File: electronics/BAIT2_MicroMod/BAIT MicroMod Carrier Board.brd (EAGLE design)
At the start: 92.7 x 80 mm, 142 parts, among them J1 SJ-43516-SMT, J10 QWIIC_RIGHT_ANGLE, J15 BM05B-SRSS-TB(LF)(SN), J2 ST-TF-003A, J4 BM05B-SRSS-TB(LF)(SN), J5 QWIIC_RIGHT_ANGLE, J6 JST 2PH, J7 MICROMOD-2222-C, SW1 SKQGADE010, SW2 SKQGADE010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

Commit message: Also removed LR_SEL from MicroMod schematic
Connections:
- removed net LR_SEL: J7.73
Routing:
- net LR_SEL: track 12.5 -> 0.00 mm
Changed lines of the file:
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@@
 <wire x1="63.107" y1="50.431" x2="63.107" y2="48.26" width="0.2032" layer="1"/>
-</signal>
-<signal name="LR_SEL">
-<contactref element="J7" pad="73"/>
-<wire x1="23" y1="49.335" x2="22.904" y2="49.239" width="0.2032" layer="1"/>
-<wire x1="22.904" y1="49.239" x2="22.904" y2="48.4547875" width="0.2032" layer="1"/>
-<wire x1="22.1278125" y1="47.6786" x2="22.904" y2="48.4547875" width="0.2032" layer="1"/>
-<wire x1="12.145" y1="48.801" x2="13.2674" y2="47.6786" width="0.2032" layer="1"/>
-<wire x1="13.2674" y1="47.6786" x2="22.1278125" y2="47.6786" width="0.2032" layer="1"/>
 </signal>
 <signal name="I2S_SCK">

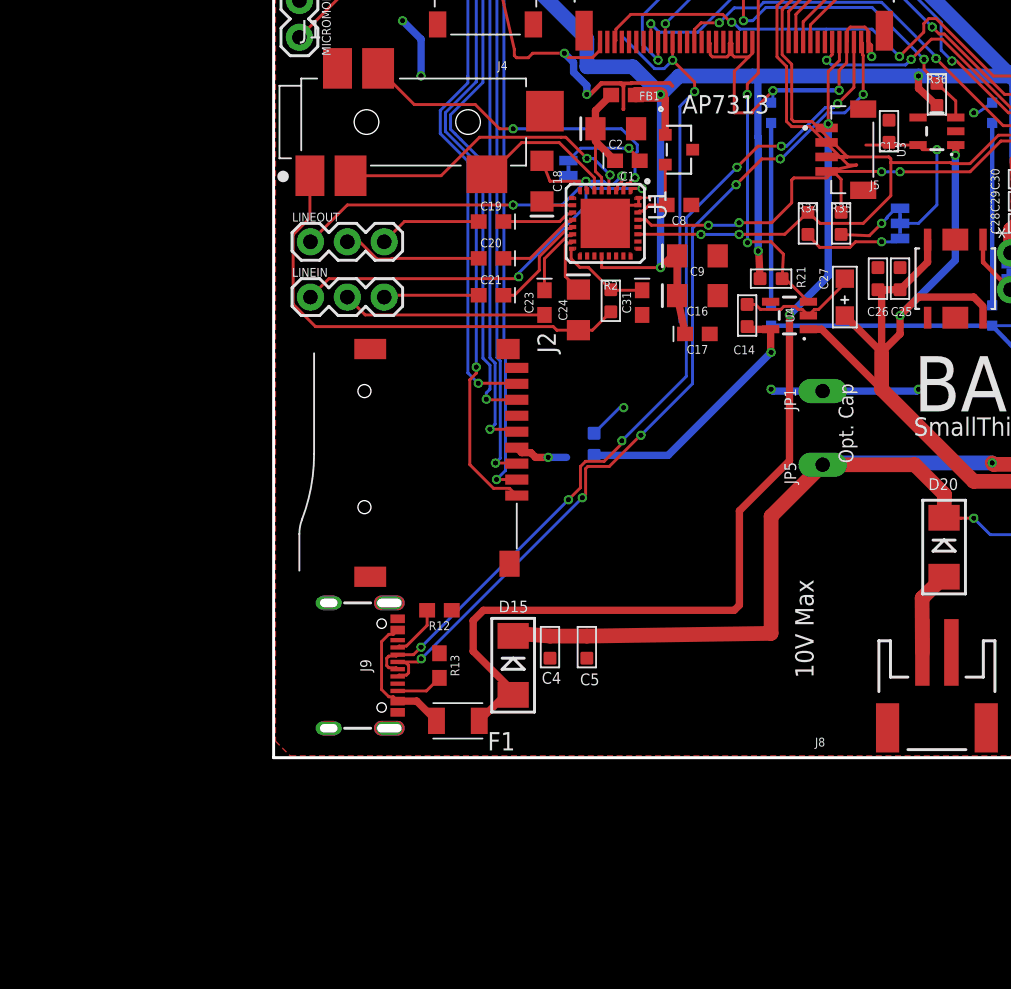
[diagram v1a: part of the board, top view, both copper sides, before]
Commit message: Added 3V3 regulators and options to power direct from 3V3 line
Added a regulator for the SGTL5000 and renamed lines from the SD and qwiic regulators. Added enable lines and jumpers to bypass the regulators if necessary.
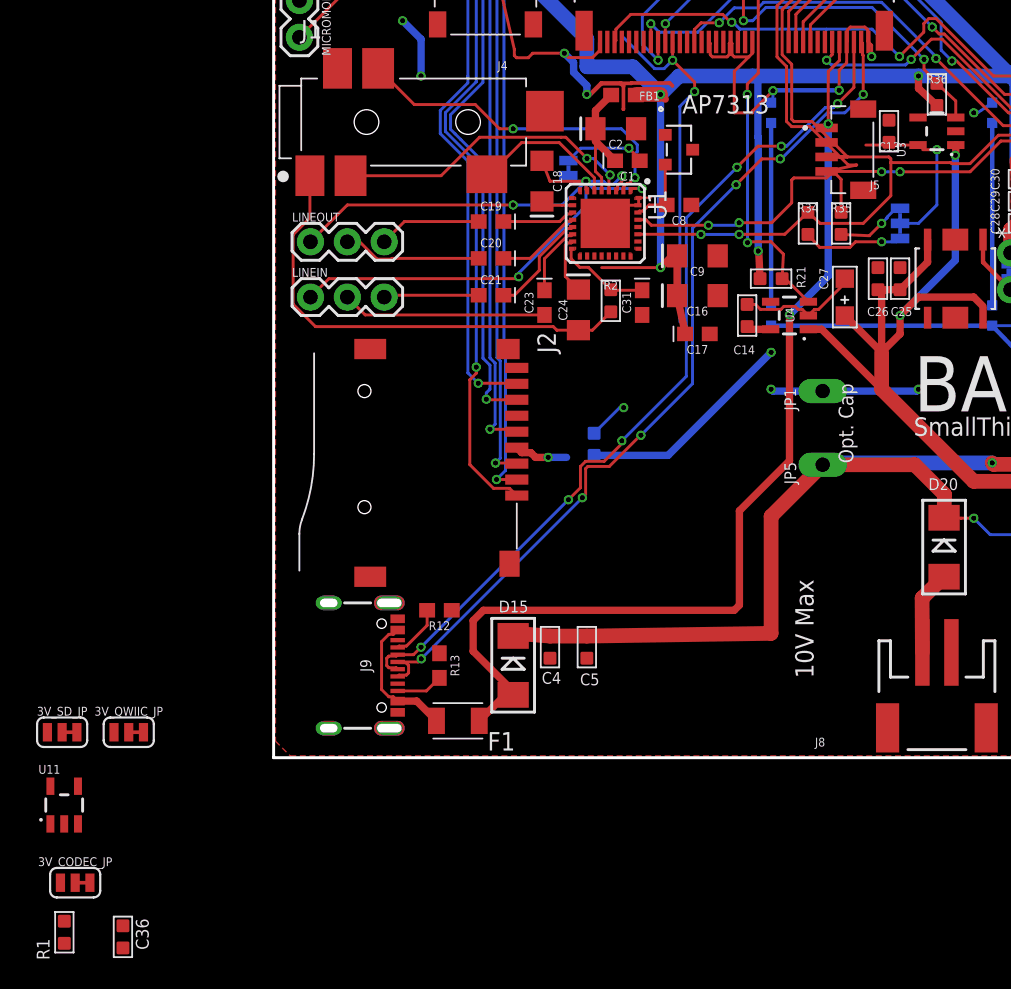
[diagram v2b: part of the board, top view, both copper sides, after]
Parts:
- added 3V_CODEC_JP, 3V_QWIIC_JP, 3V_SD_JP: MK2_LR, SparkFun-Jumpers:SMT-JUMPER_3_1-NC_TRACE_SILK
- added C36: 1uf, OPL_Capacitor:C0603
- added R1: 100K, OPL_Resistor:R0603
- added U11: 3.3V, SparkFun-IC-Power:SOT23-5
- renumbered QWIIC_PWR to QWIIC_PU
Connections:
- net PERIPHERAL_PWR_CTRL renamed SD_EN
- net QWIIC_PWR_CTRL renamed QWIIC_EN
- removed net 3.3V_LP: C14.1, C6.1, J2.4, U4.5
- removed net QWIIC_PWR: C13.1, J5.2, QWIIC_PU.2, U3.5
- new net 3V_CODEC: 3V_CODEC_JP.3, C16.+, C17.+, C9.+, FB1.1, U1.20, U2.1
- new net 3V_QWIIC: 3V_QWIIC_JP.3, J5.2, QWIIC_PU.2
- new net 3V_QWIIC_OUT: 3V_QWIIC_JP.2, C13.1, U3.5
- new net 3V_QWIIC_OUT1: 3V_CODEC_JP.2, C36.1, U11.5
- new net 3V_SD: 3V_SD_JP.3, C6.1, J2.4
- new net 3V_SD_OUT: 3V_SD_JP.2, C14.1, U4.5
- new net CODEC_EN: J7.46, R1.1, U11.3
- net 3.3V: now also 3V_CODEC_JP.1, 3V_QWIIC_JP.1, 3V_SD_JP.1, R1.2; no longer C16.+, C17.+, C9.+, FB1.1, U1.20, U2.1
- net GND: now also C36.2, U11.2
- net V+: now also U11.1
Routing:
- net 3.3V_LP: track 22.2 -> 0.00 mm, vias 2 -> 0
- net 3V_SD: track 0.00 -> 18.9 mm, vias 0 -> 2
- net QWIIC_PWR: track 12.1 -> 0.00 mm, vias 1 -> 0
- net 3.3V: track 265.9 -> 256.8 mm
- net 3V_QWIIC: track 0.00 -> 7.86 mm, vias 0 -> 1
- net 3V_CODEC: track 0.00 -> 5.44 mm
- net 3V_QWIIC_OUT: track 0.00 -> 3.81 mm
- net 3V_SD_OUT: track 0.00 -> 1.43 mm

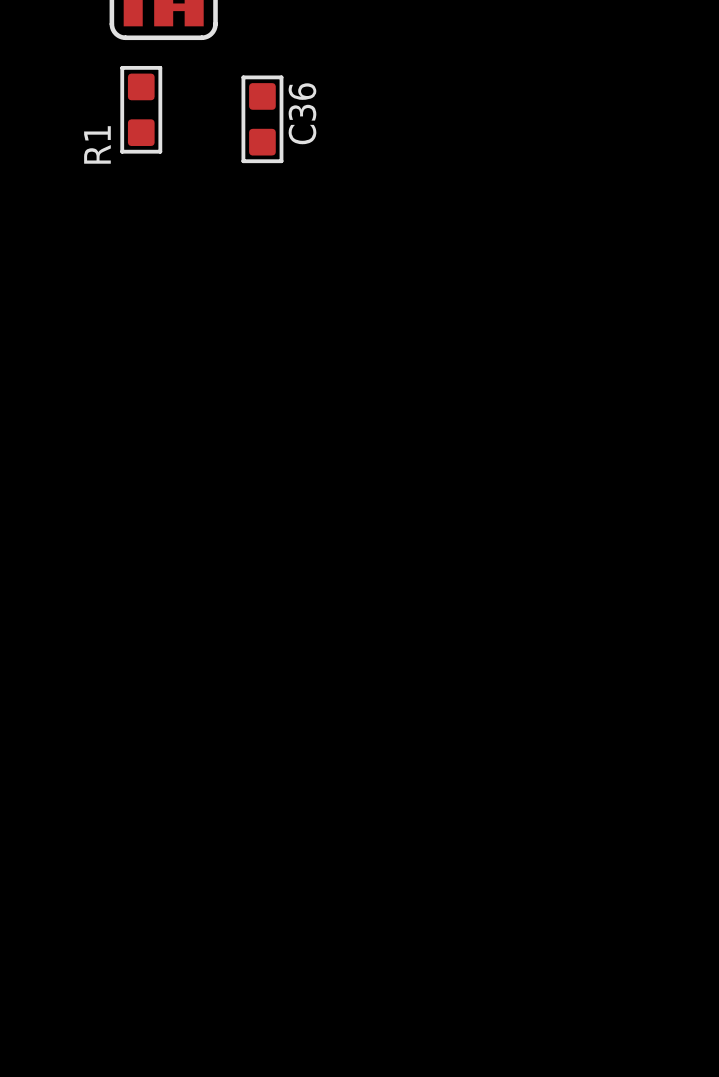
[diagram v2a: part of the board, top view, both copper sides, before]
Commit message: Added second Qwiic port, connected to I2C2 (teensy)
Also added power control for this qwiic
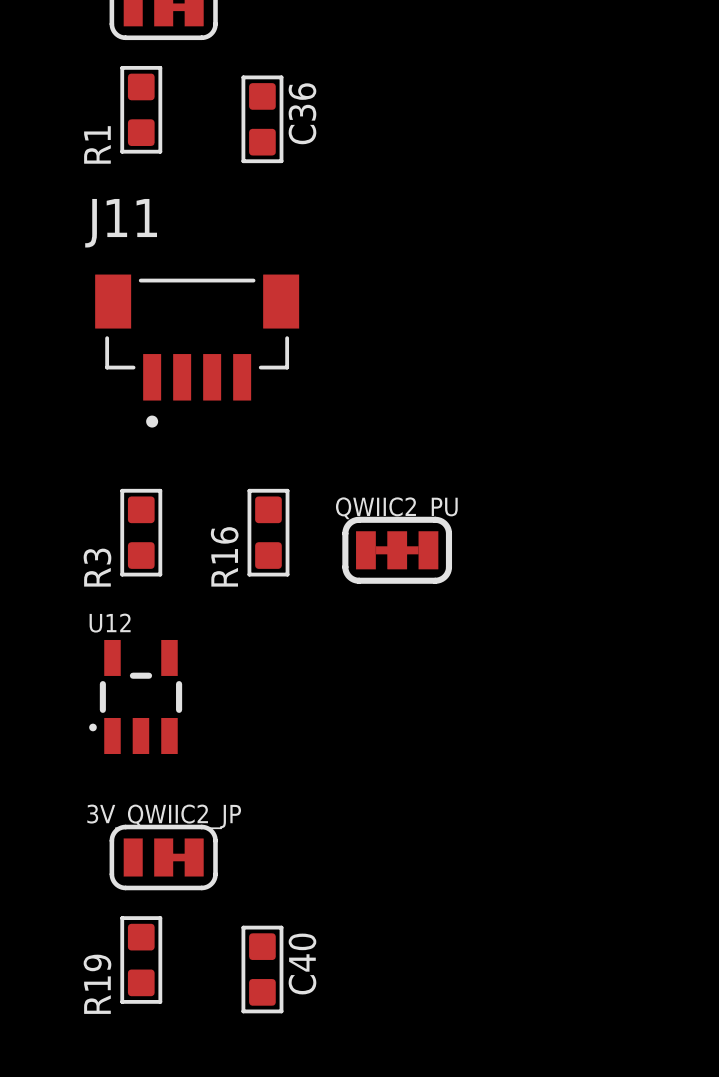
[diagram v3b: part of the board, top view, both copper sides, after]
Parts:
- added 3V_QWIIC2_JP: MK2_LR, SparkFun-Jumpers:SMT-JUMPER_3_1-NC_TRACE_SILK
- added C40: 1uf, OPL_Capacitor:C0603
- added J11: QWIIC_RIGHT_ANGLE, JST SH Connectors:JST_BM04B-SRSS-TB(LF)(SN)
- added QWIIC2_PU: (no value), SparkFun-Jumpers:SMT-JUMPER_3_2-NC_TRACE_SILK
- added R16, R3: 2.2K, OPL_Resistor:R0603
- added R19: 100K, OPL_Resistor:R0603
- added U12: 3.3V, SparkFun-IC-Power:SOT23-5
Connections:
- new net 3V_QWIIC2: 3V_QWIIC2_JP.3, J11.2, QWIIC2_PU.2
- new net 3V_QWIIC_OUT2: 3V_QWIIC2_JP.2, C40.1, U12.5
- new net I2C1_SCL: J11.4, J7.53, R16.1
- new net I2C1_SDA: J7.51
- new net I2C2_SDA: J11.3, R3.1
- new net N$1: QWIIC2_PU.3, R16.2
- new net N$2: QWIIC2_PU.1, R3.2
- new net QWIIC2_EN: J7.46, R19.1, U12.3
- net 3.3V: now also 3V_QWIIC2_JP.1, R19.2
- net CODEC_EN: now also J7.48; no longer J7.46
- net GND: now also C40.2, J11.1, J11.S1, J11.S2, U12.2
- net V+: now also U12.1
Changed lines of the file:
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@@
 <attribute name="VALUE" x="-13.679" y="-9.759" size="0.6096" layer="27" font="vector" ratio="20" align="top-center"/>
+</element>
+<element name="J11" library="JST SH Connectors" library_urn="urn:adsk.eagle:library:41161668" package="JST_BM04B-SRSS-TB(LF)(SN)" package3d_urn="urn:adsk.eagle:package:41161644/2" value="QWIIC_RIGHT_ANGLE" x="-12.564" y="-18.425" smashed="yes">
+<attribute name="AVAILABILITY" value="In Stock" x="-20.398" y="-8.202" size="1.778" layer="27" display="off"/>
+<attribute name="DESCRIPTION" value=" Connector Header Surface Mount 4 position 0.039 (1.00mm) " x="-20.398" y="-8.202" size="1.778" layer="27" display="off"/>
+<attribute name="MF" value="JST Sales" x="-20.398" y="-8.202" size="1.778" layer="27" display="off"/>
+<attribute name="MP" value="BM04B-SRSS-TB(LF)(SN)" x="-20.398" y="-8.202" size="1.778" layer="27" display="off"/>
+<attribute name="MPN" value="BM04B-SRSS-TB(LF)(SN)" x="-20.398" y="-8.202" size="1.778" layer="27" display="off"/>
+<attribute name="NAME" x="-16.214" y="-16.275" size="1.27" layer="25"/>
+<attribute name="PACKAGE" value="None" x="-20.398" y="-8.202" size="1.778" layer="27" display="off"/>
+<attribute name="PRICE" value="None" x="-20.398" y="-8.202" size="1.778" layer="27" display="off"/>
+<attribute name="PURCHASE-URL" value="https://pricing.snapeda.com/search?q=BM04B-SRSS-TB(LF)(SN)&amp;ref=eda" x="-20.398" y="-8.202" size="1.778" layer="27" display="off"/>
+<attribute name="VALUE" x="-16.214" y="-22.975" size="1.27" layer="27" align="top-left"/>
+</element>
+<element name="QWIIC2_PU" library="SparkFun-Jumpers" package="SMT-JUMPER_3_2-NC_TRACE_SILK" package3d_urn="urn:adsk.eagle:package:39289/1" value="" x="-5.896" y="-26.716" smashed="yes">
+<attribute name="NAME" x="-5.896" y="-25.573" size="0.6096" layer="25" font="vector" ratio="20" align="bottom-center"/>
+<attribute name="VALUE" x="-5.896" y="-27.859" size="0.6096" layer="27" font="vector" ratio="20" align="top-center"/>
+</element>
+<element name="R3" library="OPL_Resistor" library_urn="urn:adsk.eagle:library:8004883" package="R0603" package3d_urn="urn:adsk.eagle:package:8004941/1" value="2.2K" x="-14.426" y="-26.129" smashed="yes">
+<attribute name="MPN" value="RC0603JR-072K2L" x="-30.675" y="-12.033" size="1.778" layer="27" display="off"/>
+<attribute name="NAME" x="-15.442" y="-28.034" size="0.889" layer="25" ratio="11" rot="R90"/>
+<attribute name="VALUE" x="-12.991" y="-27.734" size="0.635" layer="27" ratio="10" rot="R90"/>
+</element>
+<element name="R16" library="OPL_Resistor" library_urn="urn:adsk.eagle:library:8004883" package="R0603" package3d_urn="urn:adsk.eagle:package:8004941/1" value="2.2K" x="-10.186" y="-26.129" smashed="yes">
+<attribute name="MPN" value="RC0603JR-072K2L" x="-34.915" y="-12.033" size="1.778" layer="27" display="off"/>
+<attribute name="NAME" x="-11.202" y="-28.034" size="0.889" layer="25" ratio="11" rot="R90"/>
+<attribute name="VALUE" x="-8.751" y="-27.734" size="0.635" layer="27" ratio="10" rot="R90"/>
+</element>
+<element name="C40" library="OPL_Capacitor" library_urn="urn:adsk.eagle:library:8004261" package="C0603" package3d_urn="urn:adsk.eagle:package:8004287/1" value="1uf" x="-10.387" y="-40.69" smashed="yes">
+<attribute name="MPN" value="CC0603KRX7R8BB105" x="-18.892" y="-25.524" size="1.778" layer="27" display="off"/>
+<attribute name="NAME" x="-10.641" y="-39.42" size="0.635" layer="33" ratio="10" rot="R270"/>
+<attribute name="NAME" x="-9.498" y="-39.42" size="0.889" layer="25" ratio="11" rot="R270"/>
+<attribute name="VALUE" x="-11.9745" y="-39.42" size="0.635" layer="27" ratio="10" rot="R270"/>
+</element>
+<element name="R19" library="OPL_Resistor" library_urn="urn:adsk.eagle:library:8004883" package="R0603" package3d_urn="urn:adsk.eagle:package:8004941/1" value="100K" x="-14.426" y="-40.373" smashed="yes">
+<attribute name="MPN" value="RC0603FR-07100KL" x="-22.931" y="-26.129" size="1.778" layer="27" display="off"/>
+<attribute name="NAME" x="-15.442" y="-42.278" size="0.889" layer="25" ratio="11" rot="R90"/>
+<attribute name="VALUE" x="-12.991" y="-41.978" size="0.635" layer="27" ratio="10" rot="R90"/>
+</element>
+<element name="U12" library="SparkFun-IC-Power" package="SOT23-5" value="3.3V" x="-14.436" y="-31.606" smashed="yes">
+<attribute name="NAME" x="-16.214" y="-29.447" size="0.6096" layer="25" ratio="20"/>
+<attribute name="PROD_ID" value="VREG-12457" x="-26.785" y="-25.24" size="1.778" layer="27" display="off"/>
+<attribute name="VALUE" x="-16.214" y="-34.4" size="0.6096" layer="27" ratio="20"/>
+</element>
+<element name="3V_QWIIC2_JP" library="SparkFun-Jumpers" library_urn="urn:adsk.eagle:library:528" package="SMT-JUMPER_3_1-NC_TRACE_SILK" package3d_urn="urn:adsk.eagle:package:39288/1" value="MK2_LR" x="-13.679" y="-36.956" smashed="yes">
+<attribute name="NAME" x="-13.679" y="-35.813" size="0.6096" layer="25" font="vector" ratio="20" align="bottom-center"/>
+<attribute name="VALUE" x="-13.679" y="-38.099" size="0.6096" layer="27" font="vector" ratio="20" align="top-center"/>
 </element>
 </elements>
@@
 <contactref element="C36" pad="2"/>
 <contactref element="U11" pad="2"/>
+<contactref element="J11" pad="1"/>
+<contactref element="J11" pad="S1"/>
+<contactref element="J11" pad="S2"/>
+<contactref element="C40" pad="2"/>
+<contactref element="U12" pad="2"/>
 <wire x1="69.5" y1="63.54" x2="67.25" y2="72.04" width="0" layer="19" extent="1-1"/>
 <wire x1="57.912" y1="73.66" x2="67.25" y2="72.04" width="0" layer="19" extent="1-1"/>
@@
 <wire x1="-14.436" y1="-4.5661" x2="8.55" y2="3.125" width="0" layer="19" extent="1-1"/>
 <wire x1="-10.387" y1="-13.112" x2="-14.436" y2="-4.5661" width="0" layer="19" extent="1-1"/>
+<wire x1="-9.764" y1="-18.425" x2="-10.387" y2="-13.112" width="0" layer="19" extent="1-1"/>
+<wire x1="-14.064" y1="-20.95" x2="-9.764" y2="-18.425" width="0" layer="19" extent="1-1"/>
+<wire x1="-15.364" y1="-18.425" x2="-14.064" y2="-20.95" width="0" layer="19" extent="1-1"/>
+<wire x1="-14.436" y1="-32.9061" x2="-14.064" y2="-20.95" width="0" layer="19" extent="1-1"/>
+<wire x1="-10.387" y1="-41.452" x2="-14.436" y2="-32.9061" width="0" layer="19" extent="1-1"/>
 </signal>
 <signal name="3.3V" class="1">
@@
 <contactref element="R1" pad="2"/>
 <contactref element="3V_CODEC_JP" pad="1"/>
+<contactref element="R19" pad="2"/>
+<contactref element="3V_QWIIC2_JP" pad="1"/>
 <wire x1="-11.004" y1="1.755" x2="22.61" y2="33.782" width="0" layer="19" extent="1-1"/>
 <wire x1="-15.593" y1="1.755" x2="-11.004" y2="1.755" width="0" layer="19" extent="1-1"/>
 <wire x1="-14.695" y1="-8.616" x2="-15.593" y2="1.755" width="0" layer="19" extent="1-1"/>
 <wire x1="-14.426" y1="-12.795" x2="-14.695" y2="-8.616" width="0" layer="19" extent="1-1"/>
+<wire x1="-14.695" y1="-36.956" x2="-14.426" y2="-12.795" width="0" layer="19" extent="1-1"/>
+<wire x1="-14.426" y1="-41.135" x2="-14.695" y2="-36.956" width="0" layer="19" extent="1-1"/>
 </signal>
 <signal name="USB_D-">
@@
 <wire x1="45.08" y1="34.158" x2="43.18" y2="32.258" width="0.508" layer="1"/>
 <contactref element="U11" pad="1"/>
+<contactref element="U12" pad="1"/>
 <wire x1="-15.386" y1="-4.5661" x2="36.8601" y2="29.53" width="0" layer="19" extent="1-1"/>
+<wire x1="-15.386" y1="-32.9061" x2="-15.386" y2="-4.5661" width="0" layer="19" extent="1-1"/>
 </signal>
 <signal name="1.8V" class="1">
@@
 <contactref element="R1" pad="1"/>
 <contactref element="U11" pad="3"/>
-<contactref element="J7" pad="46"/>
-<wire x1="-13.486" y1="-4.5661" x2="29.75" y2="56.885" width="0" layer="19" extent="1-1"/>
+<contactref element="J7" pad="48"/>
+<wire x1="-13.486" y1="-4.5661" x2="29.25" y2="56.885" width="0" layer="19" extent="1-1"/>
 <wire x1="-14.426" y1="-11.271" x2="-13.486" y2="-4.5661" width="0" layer="19" extent="1-1"/>
 </signal>
@@
 <wire x1="-12.663" y1="-8.616" x2="22.61" y2="34.58" width="0" layer="19" extent="1-1"/>
 </signal>
+<signal name="N$1">
+<contactref element="R16" pad="2"/>
+<contactref element="QWIIC2_PU" pad="3"/>
+<wire x1="-4.8546" y1="-26.716" x2="-10.186" y2="-26.891" width="0" layer="19" extent="1-1"/>
+</signal>
+<signal name="N$2">
+<contactref element="QWIIC2_PU" pad="1"/>
+<contactref element="R3" pad="2"/>
+<wire x1="-6.9374" y1="-26.716" x2="-14.426" y2="-26.891" width="0" layer="19" extent="1-1"/>
+</signal>
+<signal name="I2C1_SCL">
+<contactref element="J7" pad="53"/>
+<contactref element="J11" pad="4"/>
+<contactref element="R16" pad="1"/>
+<wire x1="-11.064" y1="-20.95" x2="28" y2="49.335" width="0" layer="19" extent="1-1"/>
+<wire x1="-10.186" y1="-25.367" x2="-11.064" y2="-20.95" width="0" layer="19" extent="1-1"/>
+</signal>
+<signal name="I2C2_SDA">
+<contactref element="J11" pad="3"/>
+<contactref element="R3" pad="1"/>
+<wire x1="-12.064" y1="-20.95" x2="-14.426" y2="-25.367" width="0" layer="19" extent="1-1"/>
+</signal>
+<signal name="3V_QWIIC2" class="1">
+<contactref element="QWIIC2_PU" pad="2"/>
+<contactref element="3V_QWIIC2_JP" pad="3"/>
+<contactref element="J11" pad="2"/>
+<wire x1="-5.896" y1="-26.716" x2="-12.663" y2="-36.956" width="0" layer="19" extent="1-1"/>
+<wire x1="-13.064" y1="-20.95" x2="-5.896" y2="-26.716" width="0" layer="19" extent="1-1"/>
+</signal>
+<signal name="3V_QWIIC_OUT2" class="1">
+<contactref element="U12" pad="5"/>
+<contactref element="C40" pad="1"/>
+<contactref element="3V_QWIIC2_JP" pad="2"/>
+<wire x1="-13.679" y1="-36.956" x2="-10.387" y2="-39.928" width="0" layer="19" extent="1-1"/>
+<wire x1="-15.386" y1="-30.3059" x2="-13.679" y2="-36.956" width="0" layer="19" extent="1-1"/>
+</signal>
+<signal name="QWIIC2_EN">
+<contactref element="R19" pad="1"/>
+<contactref element="U12" pad="3"/>
+<contactref element="J7" pad="46"/>
+<wire x1="-13.486" y1="-32.9061" x2="29.75" y2="56.885" width="0" layer="19" extent="1-1"/>
+<wire x1="-14.426" y1="-39.611" x2="-13.486" y2="-32.9061" width="0" layer="19" extent="1-1"/>
+</signal>
+<signal name="I2C1_SDA">
+<contactref element="J7" pad="51"/>
+</signal>
 </signals>
